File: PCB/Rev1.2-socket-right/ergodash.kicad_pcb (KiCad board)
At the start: 2 copper layers, 149.9 x 127.4 mm, 83 parts, among them J1 5PIN, SW1 SW_PUSH, SW10 SW_PUSH, SW11 SW_PUSH, SW12 SW_PUSH, SW13 SW_PUSH, SW14 SW_PUSH, SW15 SW_PUSH, SW16 SW_PUSH, SW17 SW_PUSH, SW18 SW_PUSH, SW19 SW_PUSH, SW2 SW_PUSH, SW20 SW_PUSH, SW21 SW_PUSH, SW22 SW_PUSH, SW23 SW_PUSH, SW24 SW_PUSH, SW25 SW_PUSH, SW26 SW_PUSH, SW27 SW_PUSH, SW28 SW_PUSH, SW29 SW_Push, SW3 SW_PUSH, SW30 SW_PUSH, SW31 SW_PUSH, SW32 SW_PUSH, SW33 SW_PUSH, SW34 SW_PUSH, SW35 SW_PUSH, SW4 SW_PUSH, SW40 SW_PUSH, SW5 SW_PUSH, SW6 SW_PUSH, SW7 SW_PUSH, SW8 SW_PUSH, SW9 SW_PUSH, U1 HOLE, U2 HOLE, U3 ProMicro, U4 HOLE, U5 HOLE, U7 HOLE, U8 HOLE, U9 HOLE

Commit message: Remove vestigial U6, add Pro Micro pin labels, refresh both boards
Schematic cleanup: delete U6 (the right-hand Pro Micro left over from the
original reversible design) from both halves' schematics. It was on_board=no
so it never appeared in the netlist or on the board; removing it just drops
dead symbols. Both schematics remain electrically identical.

Left board: add silkscreen pin-name labels (RAW/GND/RST/VCC/TX0/RX1...) around
the Pro Micro, and stamp the title block as Socket-left.

Right board: re-mirror from the left so it inherits the new pin labels and is
stamped Socket-right (mirror_right.py now swaps the title). Regenerate gerbers
and drill for both halves.

DRC: left 130 / right 131 violations (all pre-existing cosmetic/library items,
down from 137), schematic-parity 0, unrouted 0.

Co-Authored-By: Claude Opus 4.8 <noreply@anthropic.com>
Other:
- board text added: "GND"
- board text added: "RAW"
- board text added: "RST"
- board text added: "RX1"
- board text added: "TX0"
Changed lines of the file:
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@@
 	(paper "A4")
 	(title_block
-		(title "ErgoDash Rev2")
-		(date "2018-06-07")
-		(rev "2.0")
-		(company "Omkbd")
+		(title "ErgoDash Rev2 Socket-right")
+		(date "2026-06-13")
+		(rev "2.1")
+		(company "tsubu")
 	)
 	(layers
@@
 		(layer "Edge.Cuts")
 	)
+	(gr_text "RAW"
+		(at 149.872232 39.756 -0)
+		(layer "F.SilkS")
+		(effects
+			(font
+				(size 1 1)
+				(thickness 0.15)
+			)
+			(justify left bottom)
+		)
+	)
+	(gr_text "GND"
+		(at 149.872232 42.256 -0)
+		(layer "F.SilkS")
+		(effects
+			(font
+				(size 1 1)
+				(thickness 0.15)
+			)
+			(justify left bottom)
+		)
+	)
+	(gr_text "RST"
+		(at 150.372232 45.256 -0)
+		(layer "F.SilkS")
+		(effects
+			(font
+				(size 1 1)
+				(thickness 0.15)
+			)
+			(justify left bottom)
+		)
+	)
+	(gr_text "TX0"
+		(at 171.372232 39.756 -0)
+		(layer "F.SilkS")
+		(effects
+			(font
+				(size 1 1)
+				(thickness 0.15)
+			)
+			(justify left bottom)
+		)
+	)
+	(gr_text "RX1"
+		(at 171.372232 42.256 -0)
+		(layer "F.SilkS")
+		(effects
+			(font
+				(size 1 1)
+				(thickness 0.15)
+			)
+			(justify left bottom)
+		)
+	)
+	(gr_text "GND"
+		(at 171.372232 44.756 -0)
+		(layer "F.SilkS")
+		(effects
+			(font
+				(size 1 1)
+				(thickness 0.15)
+			)
+			(justify left bottom)
+		)
+	)
 	(gr_text "ErgoDash Rev. 1.2\nSocketed by tsubu"
 		(at 154.712232 139.7 -0)
@@
 	)
 	(gr_text "Designed\nby omkbd"
-		(at 196.478 139.319 -0)
+		(at 194.872232 139.756 -0)
 		(layer "F.SilkS")
 		(effects
@@
 		)
 	)
+	(gr_text "RAW"
+		(at 153.372232 39.756 -0)
+		(layer "B.SilkS")
+		(effects
+			(font
+				(size 1 1)
+				(thickness 0.15)
+			)
+			(justify left bottom mirror)
+		)
+	)
+	(gr_text "GND"
+		(at 153.372232 42.256 -0)
+		(layer "B.SilkS")
+		(effects
+			(font
+				(size 1 1)
+				(thickness 0.15)
+			)
+			(justify left bottom mirror)
+		)
+	)
+	(gr_text "RST"
+		(at 153.372232 45.256 -0)
+		(layer "B.SilkS")
+		(effects
+			(font
+				(size 1 1)
+				(thickness 0.15)
+			)
+			(justify left bottom mirror)
+		)
+	)
+	(gr_text "TX0"
+		(at 173.872232 39.756 -0)
+		(layer "B.SilkS")
+		(effects
+			(font
+				(size 1 1)
+				(thickness 0.15)
+			)
+			(justify left bottom mirror)
+		)
+	)
+	(gr_text "RX1"
+		(at 174.372232 42.256 -0)
+		(layer "B.SilkS")
+		(effects
+			(font
+				(size 1 1)
+				(thickness 0.15)
+			)
+			(justify left bottom mirror)
+		)
+	)
+	(gr_text "GND"
+		(at 174.372232 44.756 -0)
+		(layer "B.SilkS")
+		(effects
+			(font
+				(size 1 1)
+				(thickness 0.15)
+			)
+			(justify left bottom mirror)
+		)
+	)

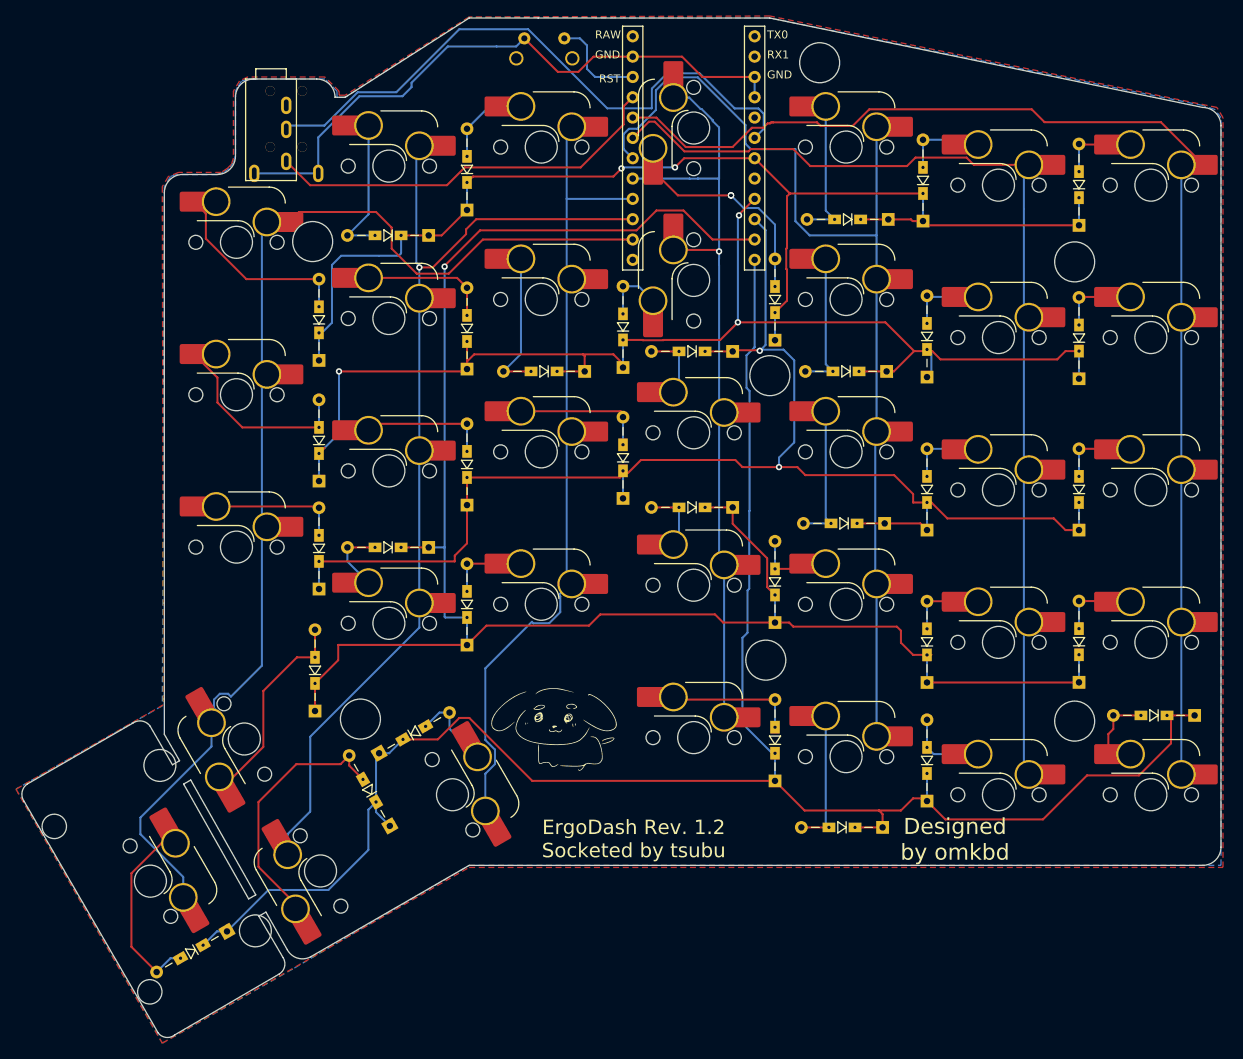
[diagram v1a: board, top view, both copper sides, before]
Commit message: Swap socket-left/right dirs to match the actual hand
The board in Rev1.2-socket-left actually builds the RIGHT hand and vice versa:
the components/sockets sit on F.Cu, which per the build guide is the underside
(裏側), so the KiCad layout is the bottom view -- mirror-reversed from use. The
inner-edge features (TRRS J1, 2U thumb SW40) are on +X, which maps to the left in
use = a right-hand half.

Swapped the two directories' contents and fixed the title blocks accordingly:
  Rev1.2-socket-right <- the active flipped-socket board (right hand, has the
                         in-progress routing)
  Rev1.2-socket-left  <- the old stale flip (NOTE: still a right-hand board, not
                         a valid left hand; to be replaced by a real left layout)

Co-Authored-By: Claude Opus 4.8 <noreply@anthropic.com>
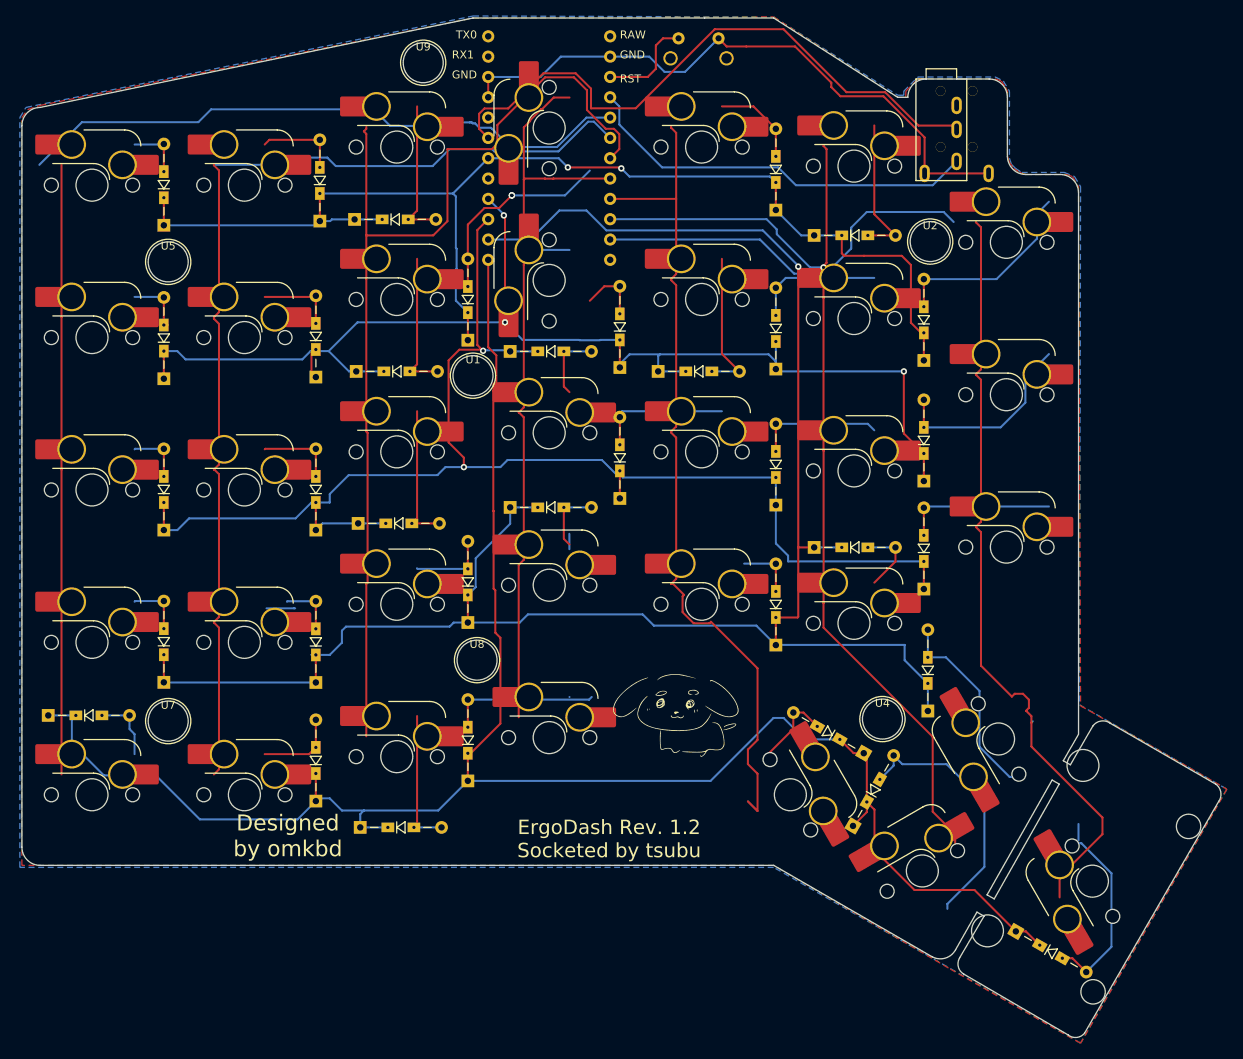
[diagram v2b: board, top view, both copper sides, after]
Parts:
- ? (x2), D1, D10, D11, D12, D13, D14, D15, D16, D17, D18, D19, D2, D20, D21, D22, D23, D24, D25, D26, D27, D28, D29, D3, D30, D31, D32, D33, D34, D4, D5, D6, D68, D7, D8, D9, J1, SW29, U1, U2, U3, U4, U5, U7, U8, U9: moved to F.Cu
- ?: moved to B.Cu
- moved D29 143.3 mm to (81.5, 124.3), turned to 0 degrees
- moved SW1 132.4 mm to (87.0, 58.0)
- moved SW2 132.4 mm to (87.0, 77.0)
- moved SW3 132.4 mm to (87.0, 96.1)
- moved SW30 132.4 mm to (87.0, 134.2)
- moved SW4 132.4 mm to (87.0, 115.1)
- moved ? 117.8 mm to (212.1, 145.0), turned to -120 degrees
- moved SW40 117.8 mm to (212.1, 145.0), turned to -60 degrees
- moved D1 114.4 mm to (96.0, 63.0)
- moved D2 114.4 mm to (96.0, 82.2)
- moved D3 114.4 mm to (96.0, 101.1)
- moved D4 114.4 mm to (96.0, 120.1)
- moved U5 113.3 mm to (96.5, 67.6), turned to 0 degrees
- moved U7 113.3 mm to (96.5, 125.0), turned to 0 degrees
- moved D68 98.6 mm to (202.5, 151.3), turned to -30 degrees
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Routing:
- net /col1: track 132.6 -> 136.2 mm
- net Net-(D8-A): track 10.7 -> 7.09 mm
- added copper zone on F.Cu, net GND
- added copper zone on B.Cu, net VCC
- removed copper zone on B.Cu, net GND
- removed copper zone on F.Cu, net VCC
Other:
- outline, holes or cut-outs redrawn

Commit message: WIP scaffold: relocate Pro Micro/reset to right-hand side (socket-right)
Rough geometry placement only (per the keys-stay-put / A approach):
- U3 (Pro Micro) -> X=163.2 on F.Cu (over the SW17/18 column)
- SW29 (reset)   -> X=144.0 on F.Cu
- SW17/SW18 -> -90 deg, SW13/SW14 -> 180 deg (revert)

This is a STARTING SCAFFOLD, not finished: SW17/SW18 sockets still collide with
the Pro Micro pin rows and must be hand-threaded between them (~0.27mm, like the
existing SW13/14), and the whole Pro Micro/reset area needs rerouting. Done by
hand in KiCad.

Co-Authored-By: Claude Opus 4.8 <noreply@anthropic.com>
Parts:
- moved U3 19.0 mm to (163.2, 53.3)
- moved SW29 18.8 mm to (144.0, 39.6)
- turned SW13 to 180 degrees
- turned SW14 to 180 degrees
- turned SW17 to -90 degrees
- turned SW18 to -90 degrees
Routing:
- net /rst: track 12.3 -> 0.00 mm
- net GND: track 78.6 -> 90.9 mm

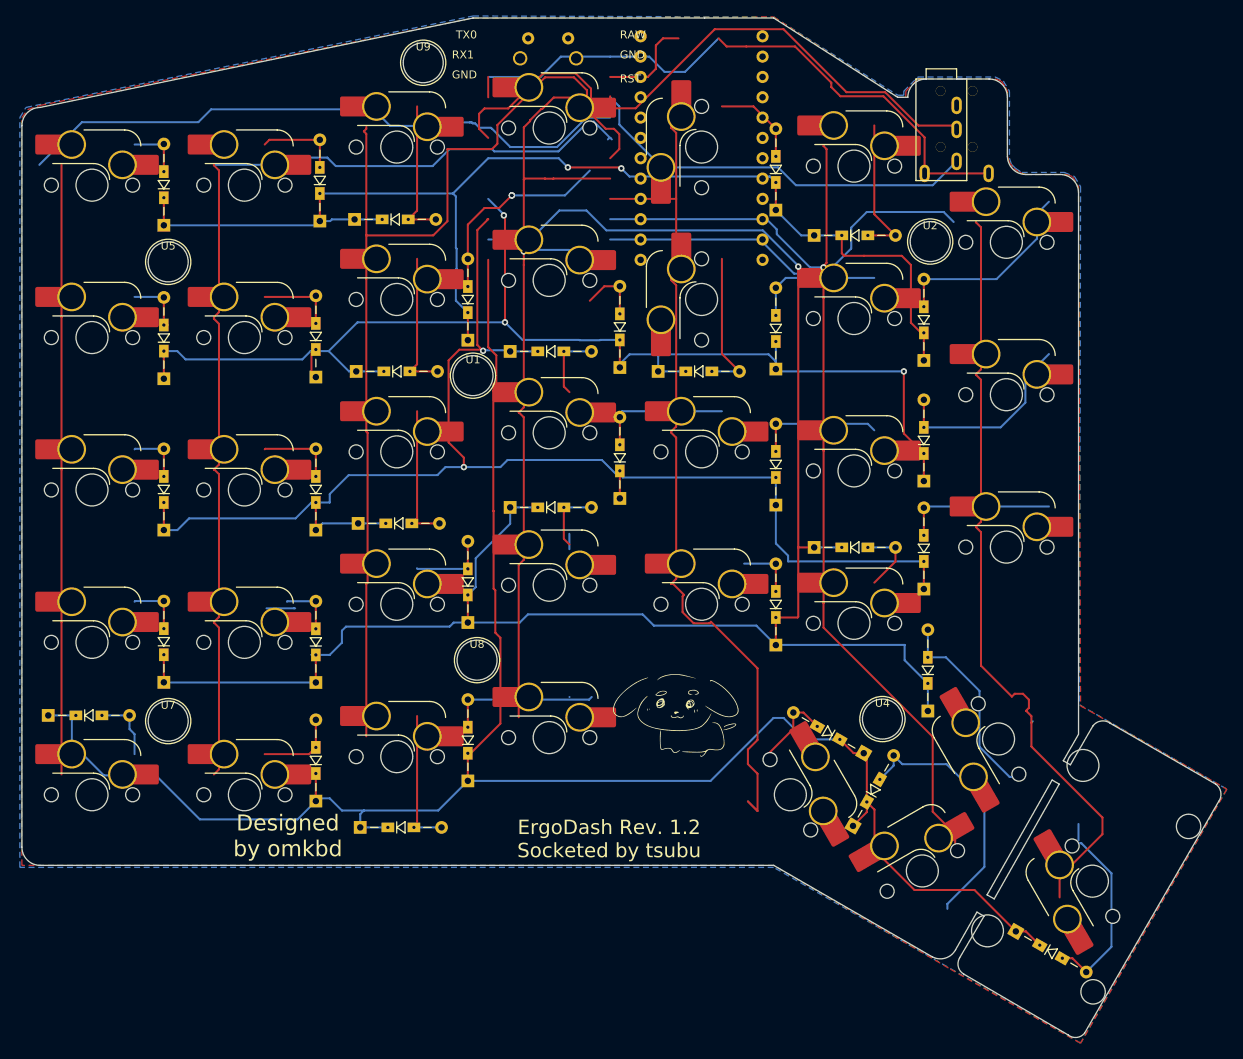
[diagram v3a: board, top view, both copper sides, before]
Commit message: Complete right-hand board routing + regenerate gerbers (socket-right)
socket-right (right hand) is now electrically complete:
- matrix fully hand-routed (0 unconnected, 0 clearance/shorting/thermal/dangling)
- Pro Micro relocated to the right-hand side (over SW17/18); SW17/18 threaded
  through its pin rows; SW13/14 reverted; reset moved
- starved_thermal fixed (GND stub into the pour)
- Default clearance relaxed to 0.2 mm (well within JLCPCB's 0.127 mm min) to
  clear the marginal pin-area clearances
- silkscreen tidied

Remaining DRC items are non-electrical (silk overlaps, lib_footprint notes, and
the socket+switch shared-footprint courtyard overlaps = same as baseline).

Gerbers + drills regenerated into ergodash/ and rezipped (was stale).

Co-Authored-By: Claude Opus 4.8 <noreply@anthropic.com>
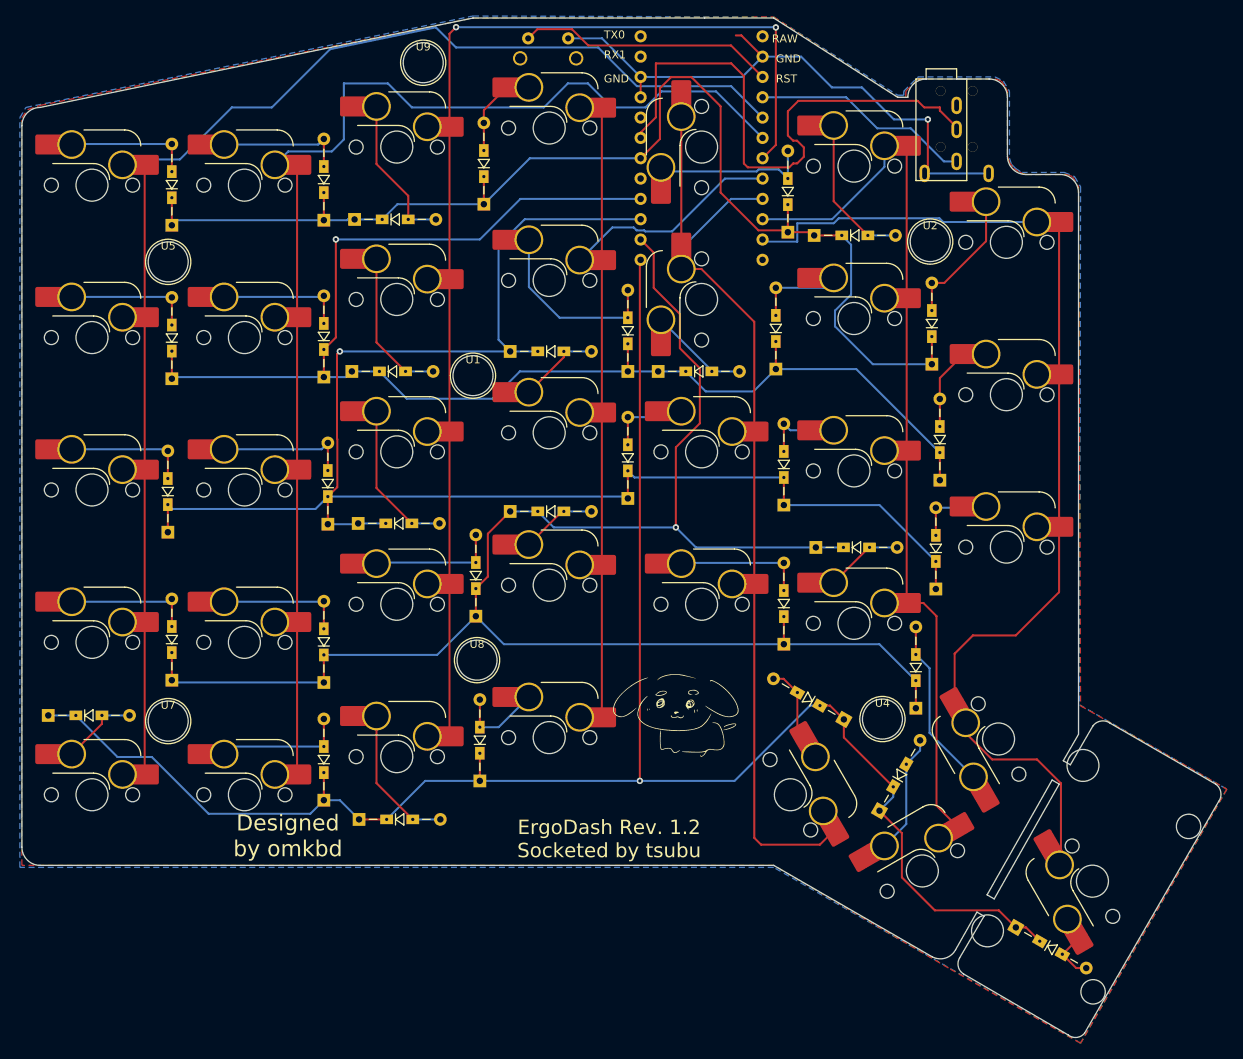
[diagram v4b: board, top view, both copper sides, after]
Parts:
- moved D13 17.1 mm to (136.0, 60.4)
- moved D33 4.90 mm to (181.0, 124.8)
- moved D34 3.81 mm to (185.4, 136.2)
- moved D17 3.15 mm to (174.0, 63.9)
- moved D26 2.00 mm to (193.0, 94.9)
- moved D7 1.67 mm to (116.5, 100.4)
- moved D28 1.54 mm to (190.0, 123.4)
- moved D27 1.50 mm to (192.5, 108.5)
- moved D32 1.50 mm to (135.5, 132.4)
- moved D12 1.28 mm to (135.0, 111.9)
- moved D14 1.11 mm to (154.0, 81.3)
- moved D25 1.11 mm to (192.0, 80.4)
- moved D4 1.03 mm to (97.0, 119.9)
- moved D31 1.01 mm to (120.4, 137.3)
- moved D30 1.01 mm to (116.0, 134.9)
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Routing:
- net /rst: track 0.00 -> 32.2 mm
- net /row2: track 176.3 -> 201.3 mm, vias 2 -> 1
- net VCC: track 50.5 -> 27.6 mm
- net /row3: track 233.2 -> 211.0 mm
- net Net-(D68-A): track 26.5 -> 6.55 mm
- net /row1: track 158.4 -> 177.5 mm, vias 3 -> 1
- net Net-(D34-A): track 32.7 -> 15.0 mm
- net GND: track 90.9 -> 73.3 mm, vias 0 -> 1
- net Net-(D13-A): track 25.8 -> 9.07 mm, vias 2 -> 0
- net /col1: track 136.2 -> 152.4 mm
- net /col2: track 130.9 -> 147.0 mm, vias 0 -> 2
- net /col5: track 125.4 -> 109.6 mm, vias 1 -> 0
- net Net-(D14-A): track 8.14 -> 23.3 mm
- net Net-(D26-A): track 24.8 -> 10.3 mm
- net /col6: track 146.1 -> 132.0 mm
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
